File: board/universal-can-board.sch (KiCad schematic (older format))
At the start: 54 parts, among them IC1 ATMEGA328P-A, P1 USB_OTG, P2 CONN_01X08, P3 CONN_01X02, P4 CONN_01X04, U1 FT232RL, U2 LM1117-3.3, U3 MCP2515-I/ST, U4 MCP2551-I/SN, Y1 Crystal_GND2, Y2 Crystal

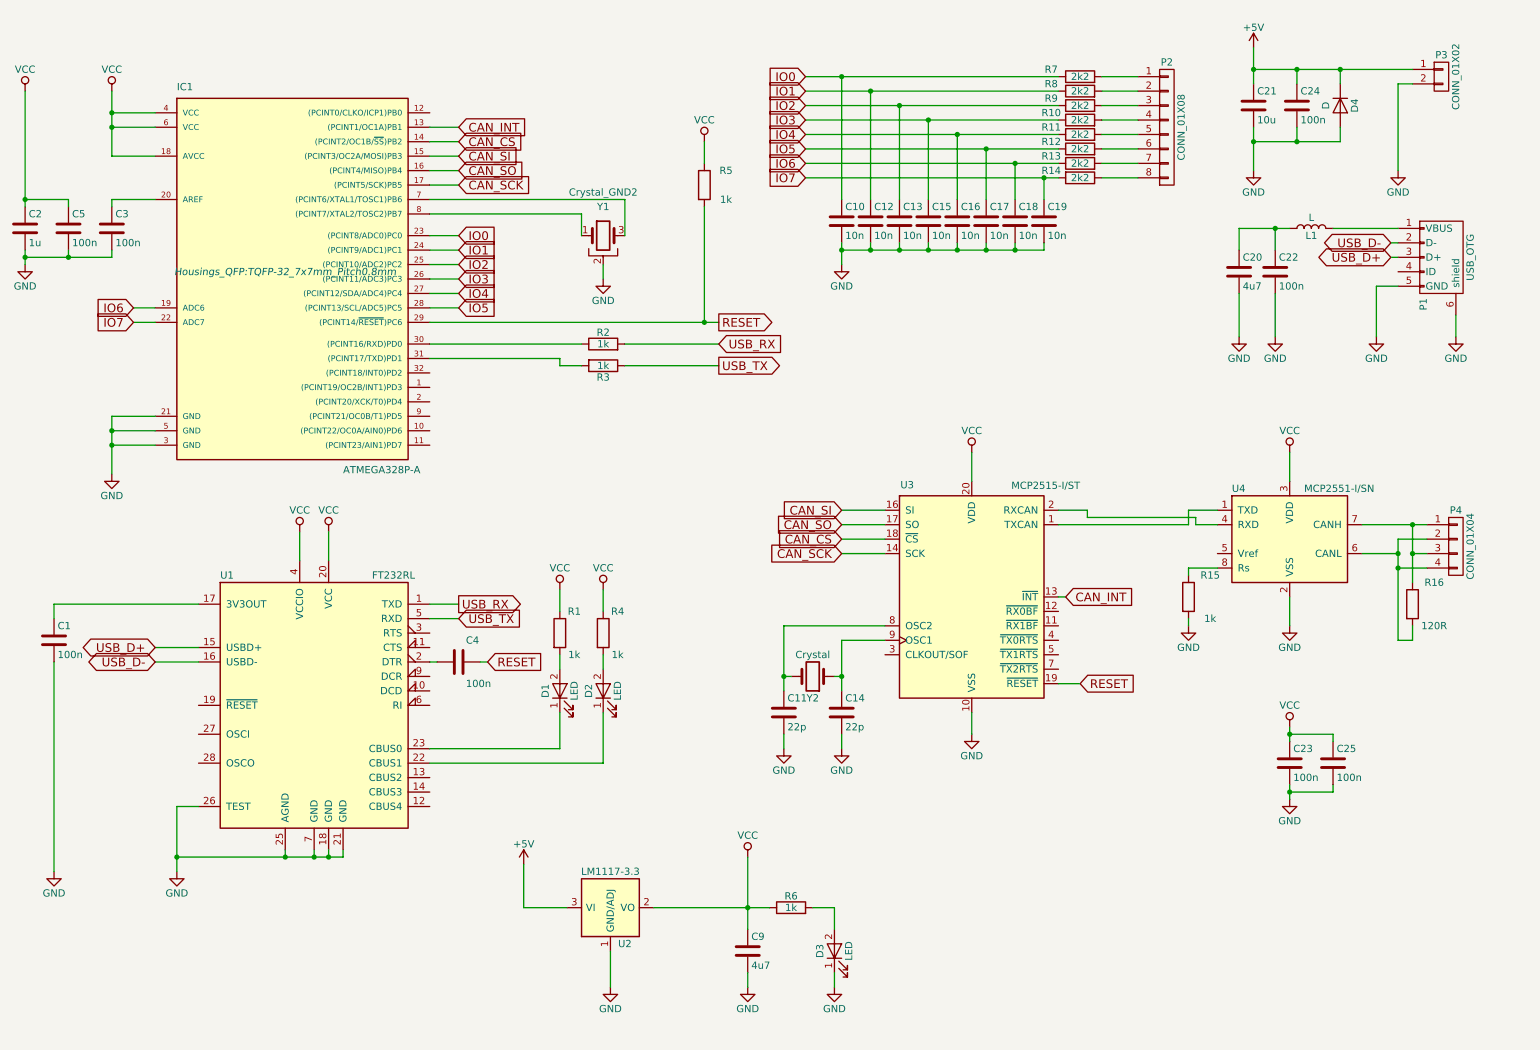
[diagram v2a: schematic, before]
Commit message: Improved input circuit protection. Started with first version of the layout.
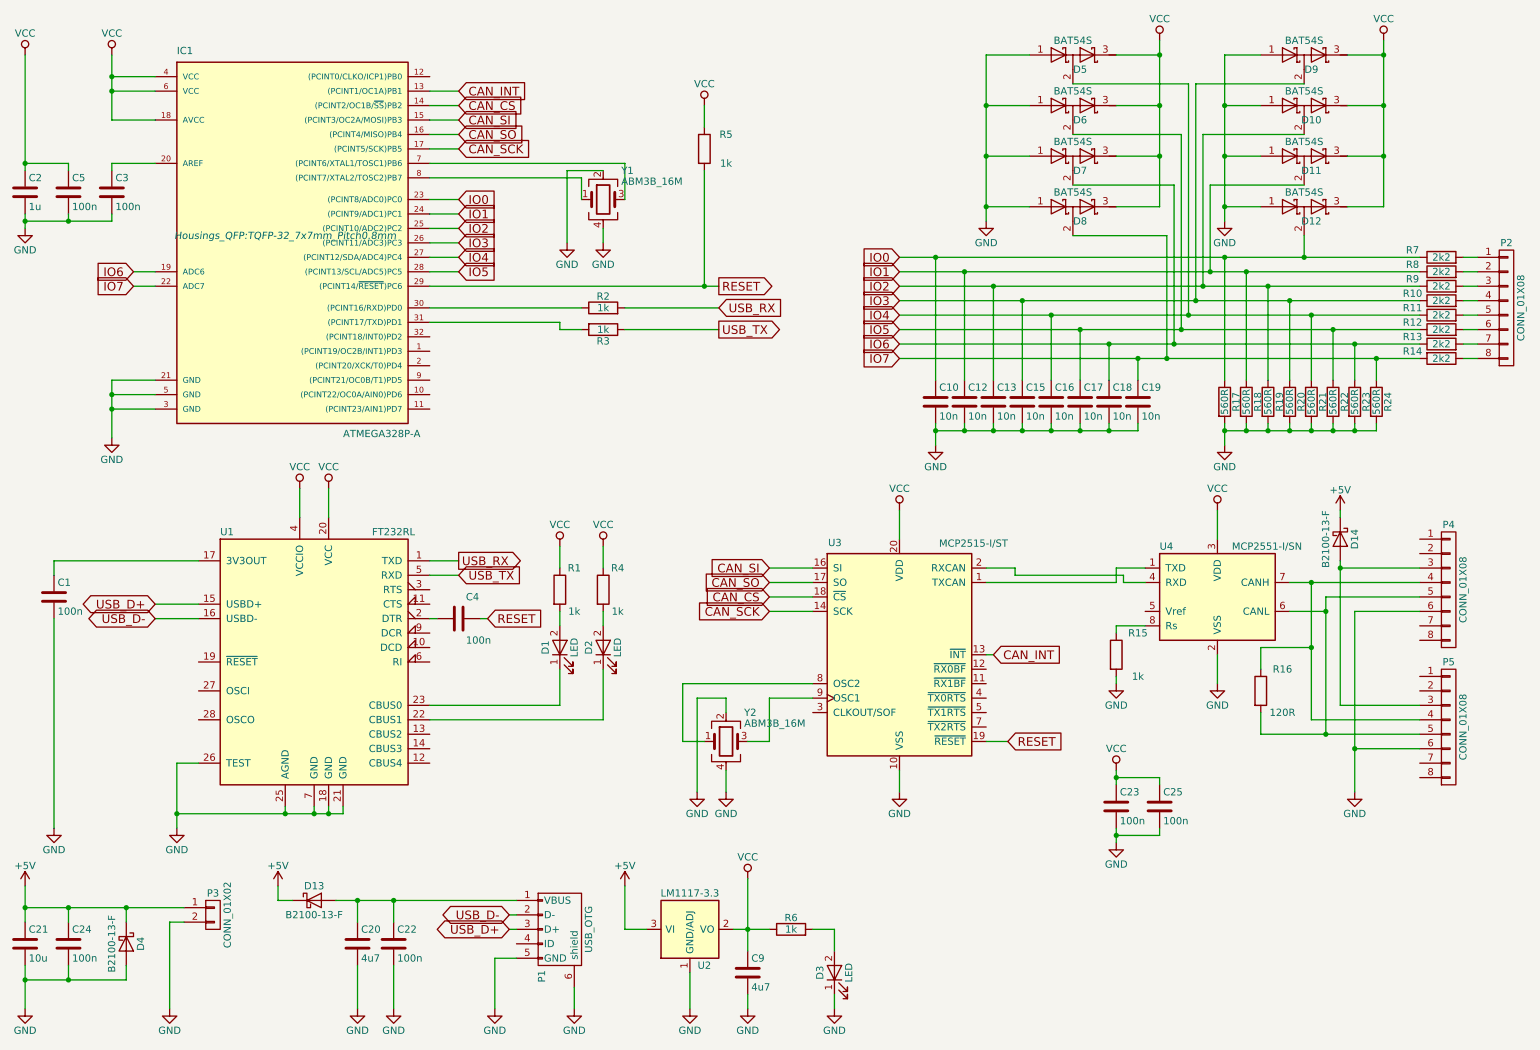
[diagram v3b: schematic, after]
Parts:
- removed C11, C14: 22p, symbol C
- removed D4: D, symbol D
- removed L1: L, symbol L
- removed P4: CONN_01X04, symbol CONN_01X04
- removed Y1: Crystal_GND2, symbol Crystal_GND2
- removed Y2: Crystal, symbol Crystal
- added D10, D11, D12, D5, D6, D7, D8, D9: BAT54S, TO_SOT_Packages_SMD:SOT-23, symbol D_Schottky_x2_Serial_ACK
- added D13, D14, D4: B2100-13-F, Diodes_SMD:SMB_Standard, symbol D_Schottky
- added P4, P5: CONN_01X08, Connector_RJ:RJ45_8, symbol CONN_01X08
- added R17, R18, R19, R20, R21, R22, R23, R24: 560R, Resistors_SMD:R_0805, symbol R
- added Y1, Y2: ABM3B_16M, Crystals:Crystal_SMD_5032_4Pads, symbol Crystal_GND24
- C1, C10, C12, C13, C15, C16, C17, C18, C19, C2, C22, C23, C24, C25, C3, C4, C5: footprint (none) -> Capacitors_SMD:C_0805
- C20, C21, C9: footprint (none) -> Capacitors_SMD:C_1210
- D1, D2, D3: footprint (none) -> LEDs:LED_0805
- P1: footprint (none) -> Connector_USB:USB_Mini-B_Lumber_2486_Horizontal
- P2: footprint (none) -> Connectors_Phoenix:PhoenixContact_MSTBVA-G_08x5.08mm_Vertical
- P3: footprint (none) -> Connectors_Phoenix:PhoenixContact_MSTBVA-G_02x5.08mm_Vertical
- R1, R10, R11, R12, R13, R14, R15, R16, R2, R3, R4, R5, R6, R7, R8, R9: footprint (none) -> Resistors_SMD:R_0805
- U2: footprint (none) -> TO_SOT_Packages_SMD:SOT-223
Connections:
- net +5V: now also D13.1 (K), D14.1 (K), D4.1 (K)
- net GND: now also D10.1 (A), D11.1 (A), D12.1 (A), D4.2 (A), D5.1 (A), D6.1 (A), D7.1 (A), D8.1 (A), D9.1 (A), P4.6 (P6), P5.6 (P6), R17.2, R18.2, R19.2, R20.2, R21.2, R22.2, R23.2, R24.2, Y1.2, Y1.4, Y2.2, Y2.4
- net IO0: now also D12.2 (common), R17.1
- net IO1: now also D11.2 (common), R18.1
- net IO2: now also D10.2 (common), R19.1
- net IO3: now also D9.2 (common), R20.1
- net IO4: now also D5.2 (common), R21.1
- net IO5: now also D6.2 (common), R22.1
- net IO6: now also D7.2 (common), R23.1
- net IO7: now also D8.2 (common), R24.1
- net VCC: now also D10.3 (K), D11.3 (K), D12.3 (K), D5.3 (K), D6.3 (K), D7.3 (K), D8.3 (K), D9.3 (K)
- net at IC1.7 ((PCINT6/XTAL1/TOSC1)PB6): now also Y1.3
- net at IC1.8 ((PCINT7/XTAL2/TOSC2)PB7): now also Y1.1
- net at P1.1 (VBUS): now also C20.1, C22.1, D13.2 (A)
- net at R16.1, U4.7 (CANH): now also P4.4 (P4), P5.4 (P4)
- net at R16.2, U4.6 (CANL): now also P4.5 (P5), P5.5 (P5)
- net at U3.8 (OSC2): now also Y2.1
- net at U3.9 (OSC1): now also Y2.3
- new net: D14.2 (A), P4.3 (P3), P5.3 (P3)
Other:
- moved on the sheet: C1, C10, C12, C13, C15, C16, C17, C18, C19, C2, C20, C21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

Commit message: Routing of board v1.1
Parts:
- added C6: 100n, Capacitors_SMD:C_0805, symbol C
- P1: symbol USB_OTG -> USB_OTG-RESCUE-universal-can-board
- U2: symbol LM1117-3.3 -> LM1117-3.3-RESCUE-universal-can-board
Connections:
- net GND: now also C6.2
- net VCC: now also C6.1
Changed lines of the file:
@@
 EESchema Schematic File Version 2
+LIBS:universal-can-board-rescue
 LIBS:power
 LIBS:device
@@
 $EndComp
 $Comp
-L USB_OTG P1
+L USB_OTG-RESCUE-universal-can-board P1
 U 1 1 5A6CECE5
 P 4450 6850
@@
 	4600 1650 4600 1800
 $Comp
-L LM1117-3.3 U2
+L LM1117-3.3-RESCUE-universal-can-board U2
 U 1 1 5A6D051D
 P 5350 6850
@@
 Wire Wire Line
 	9850 4000 9850 3950
+$Comp
+L C C6
+U 1 1 5A806EAE
+P 5050 4500
+F 0 "C6" H 5075 4600 50  0000 L CNN
+F 1 "100n" H 5075 4400 50  0000 L CNN
+F 2 "Capacitors_SMD:C_0805" H 5088 4350 50  0001 C CNN
+F 3 "" H 5050 4500 50  0001 C CNN
+	1    5050 4500
+	1    0    0    -1
+$EndComp
+$Comp
+L VCC #PWR044
+U 1 1 5A80704F
+P 5050 4200
+F 0 "#PWR044" H 5050 4050 50  0001 C CNN
+F 1 "VCC" H 5050 4350 50  0000 C CNN
+F 2 "" H 5050 4200 50  0001 C CNN
+F 3 "" H 5050 4200 50  0001 C CNN
+	1    5050 4200
+	1    0    0    -1
+$EndComp
+$Comp
+L GND #PWR045
+U 1 1 5A8070F1
+P 5050 5900
+F 0 "#PWR045" H 5050 5650 50  0001 C CNN
+F 1 "GND" H 5050 5750 50  0000 C CNN
+F 2 "" H 5050 5900 50  0001 C CNN
+F 3 "" H 5050 5900 50  0001 C CNN
+	1    5050 5900
+	1    0    0    -1
+$EndComp
+Wire Wire Line
+	5050 4650 5050 5900
+Wire Wire Line
+	5050 4200 5050 4350
 $EndSCHEMATC

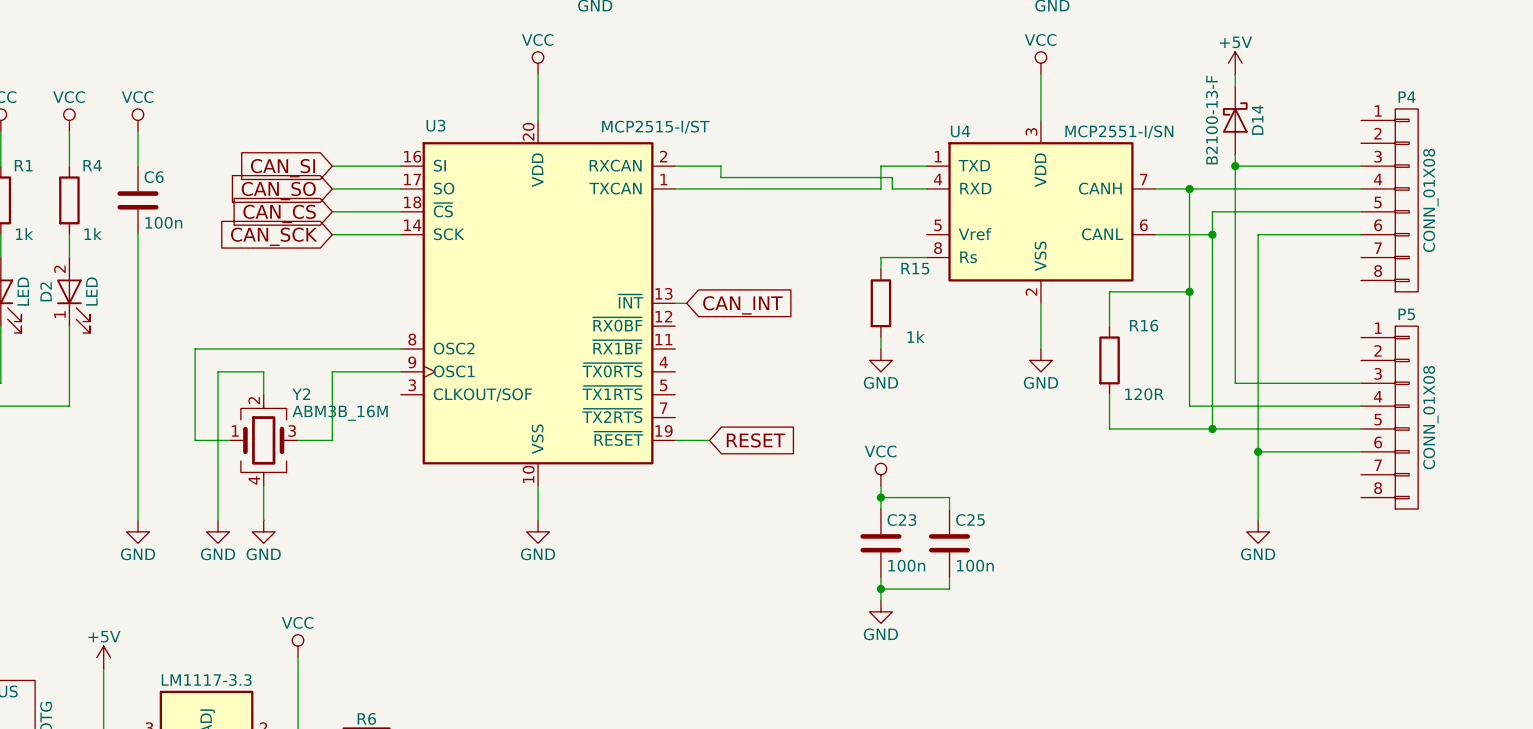
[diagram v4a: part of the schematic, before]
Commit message: Updated board layout.
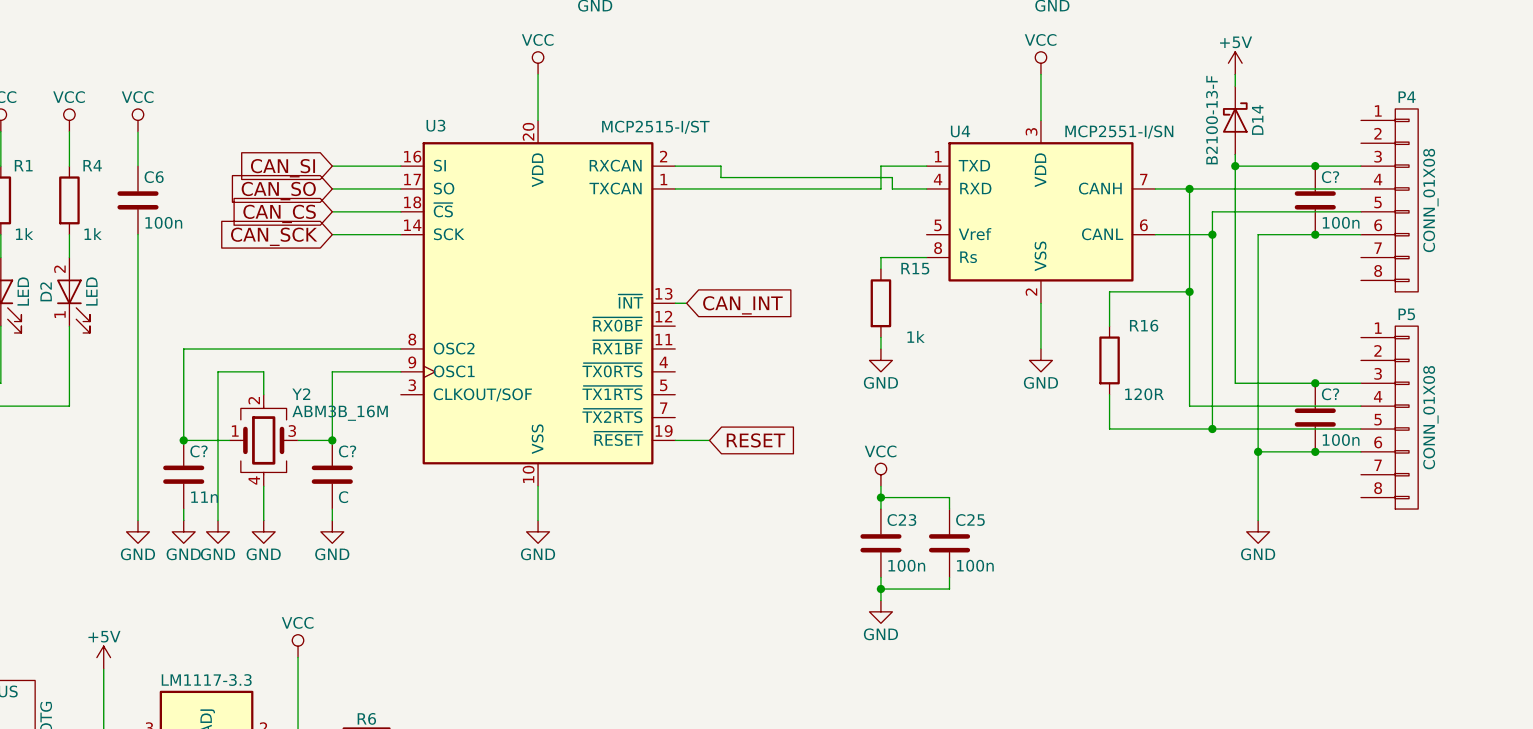
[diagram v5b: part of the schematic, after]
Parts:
- added C? (x2): 100n, symbol C
- added C?: 11n, symbol C
- added C?: C, symbol C
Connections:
- net GND: now also C?.2, C?.2, C?.2, C?.2
- net at U3.8 (OSC2), Y2.1: now also C?.1
- net at U3.9 (OSC1), Y2.3: now also C?.1
- net at D14.2 (A), P4.3 (P3), P5.3 (P3): now also C?.1, C?.1
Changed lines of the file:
@@
 	5900 5250 6200 5250
 Wire Wire Line
-	5300 5150 6200 5150
+	5250 5150 6200 5150
 Text GLabel 5900 4550 0    60   Input ~ 0
 CAN_CS
@@
 	5900 5550 5750 5550
 Wire Wire Line
-	5450 5550 5300 5550
-Wire Wire Line
-	5300 5550 5300 5150
+	5250 5550 5450 5550
 Wire Wire Line
 	5600 5900 5600 5750
@@
 Wire Wire Line
 	5050 4200 5050 4350
+$Comp
+L C C?
+U 1 1 5A831226
+P 10200 5450
+F 0 "C?" H 10225 5550 50  0000 L CNN
+F 1 "100n" H 10225 5350 50  0000 L CNN
+F 2 "" H 10238 5300 50  0001 C CNN
+F 3 "" H 10200 5450 50  0001 C CNN
+	1    10200 5450
+	1    0    0    -1
+$EndComp
+$Comp
+L C C?
+U 1 1 5A8315CF
+P 10200 4500
+F 0 "C?" H 10225 4600 50  0000 L CNN
+F 1 "100n" H 10225 4400 50  0000 L CNN
+F 2 "" H 10238 4350 50  0001 C CNN
+F 3 "" H 10200 4500 50  0001 C CNN
+	1    10200 4500
+	1    0    0    -1
+$EndComp
+Connection ~ 10200 4350
+Connection ~ 10200 4650
+Connection ~ 10200 5300
+Connection ~ 10200 5600
+Wire Wire Line
+	5250 5550 5250 5150
+$Comp
+L C C?
+U 1 1 5A832AFE
+P 5250 5700
+F 0 "C?" H 5275 5800 50  0000 L CNN
+F 1 "11n" H 5275 5600 50  0000 L CNN
+F 2 "" H 5288 5550 50  0001 C CNN
+F 3 "" H 5250 5700 50  0001 C CNN
+	1    5250 5700
+	1    0    0    -1
+$EndComp
+$Comp
+L C C?
+U 1 1 5A832BD1
+P 5900 5700
+F 0 "C?" H 5925 5800 50  0000 L CNN
+F 1 "C" H 5925 5600 50  0000 L CNN
+F 2 "" H 5938 5550 50  0001 C CNN
+F 3 "" H 5900 5700 50  0001 C CNN
+	1    5900 5700
+	1    0    0    -1
+$EndComp
+Connection ~ 5900 5550
+Connection ~ 5250 5550
+$Comp
+L GND #PWR?
+U 1 1 5A832C94
+P 5250 5900
+F 0 "#PWR?" H 5250 5650 50  0001 C CNN
+F 1 "GND" H 5250 5750 50  0000 C CNN
+F 2 "" H 5250 5900 50  0001 C CNN
+F 3 "" H 5250 5900 50  0001 C CNN
+	1    5250 5900
+	1    0    0    -1
+$EndComp
+$Comp
+L GND #PWR?
+U 1 1 5A832D3E
+P 5900 5900
+F 0 "#PWR?" H 5900 5650 50  0001 C CNN
+F 1 "GND" H 5900 5750 50  0000 C CNN
+F 2 "" H 5900 5900 50  0001 C CNN
+F 3 "" H 5900 5900 50  0001 C CNN
+	1    5900 5900
+	1    0    0    -1
+$EndComp
+Wire Wire Line
+	5250 5900 5250 5850
+Wire Wire Line
+	5900 5900 5900 5850
 $EndSCHEMATC

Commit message: Added last missing parts and changed some routings.
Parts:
- removed C24: 100n, Capacitors_SMD:C_0805, symbol C
- added C7, C8: 11p, Capacitors_SMD:C_0805, symbol C
- added SW1: SW_Push, Buttons_Switches_SMD:SW_SPST_EVQP2, symbol SW_Push
- C11: renamed from C?; value 11n -> 11p; footprint (none) -> Capacitors_SMD:C_0805
- C14: renamed from C?; value C -> 11p; footprint (none) -> Capacitors_SMD:C_0805
- C26, C27: renamed from C?; footprint (none) -> Capacitors_SMD:C_0805
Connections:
- net +5V: no longer D13.1 (K)
- net GND: now also P4.2 (P2), P4.8 (P8), P5.2 (P2), P5.8 (P8), C7.2, C8.2, SW1.2
- net RESET: now also SW1.1
- net VCC: now also D13.1 (K)
- net at IC1.7 ((PCINT6/XTAL1/TOSC1)PB6), Y1.3: now also C8.1
- net at IC1.8 ((PCINT7/XTAL2/TOSC2)PB7), Y1.1: now also C7.1
- net at P4.1 (P1): now also C26.1, C27.1, D14.2 (A), P4.3 (P3), P4.7 (P7), P5.1 (P1), P5.3 (P3), P5.7 (P7)

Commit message: Flipped input filter C (CAN) from top to bottom.
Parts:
- U2: value LM1117-3.3 -> LM1117-5.0
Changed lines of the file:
@@
 P 5350 6850
 F 0 "U2" H 5450 6600 50  0000 C CNN
-F 1 "LM1117-3.3" H 5350 7100 50  0000 C CNN
+F 1 "LM1117-5.0" H 5350 7100 50  0000 C CNN
 F 2 "TO_SOT_Packages_SMD:SOT-223" H 5350 6850 50  0001 C CNN
 F 3 "" H 5350 6850 50  0000 C CNN
